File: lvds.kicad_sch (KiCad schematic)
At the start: 31 parts, among them J4 Conn_01x22_Female, J9 Conn_01x34_Female, U10 TPS61176RTER, U5 SN65DSI83TPAPRQ1

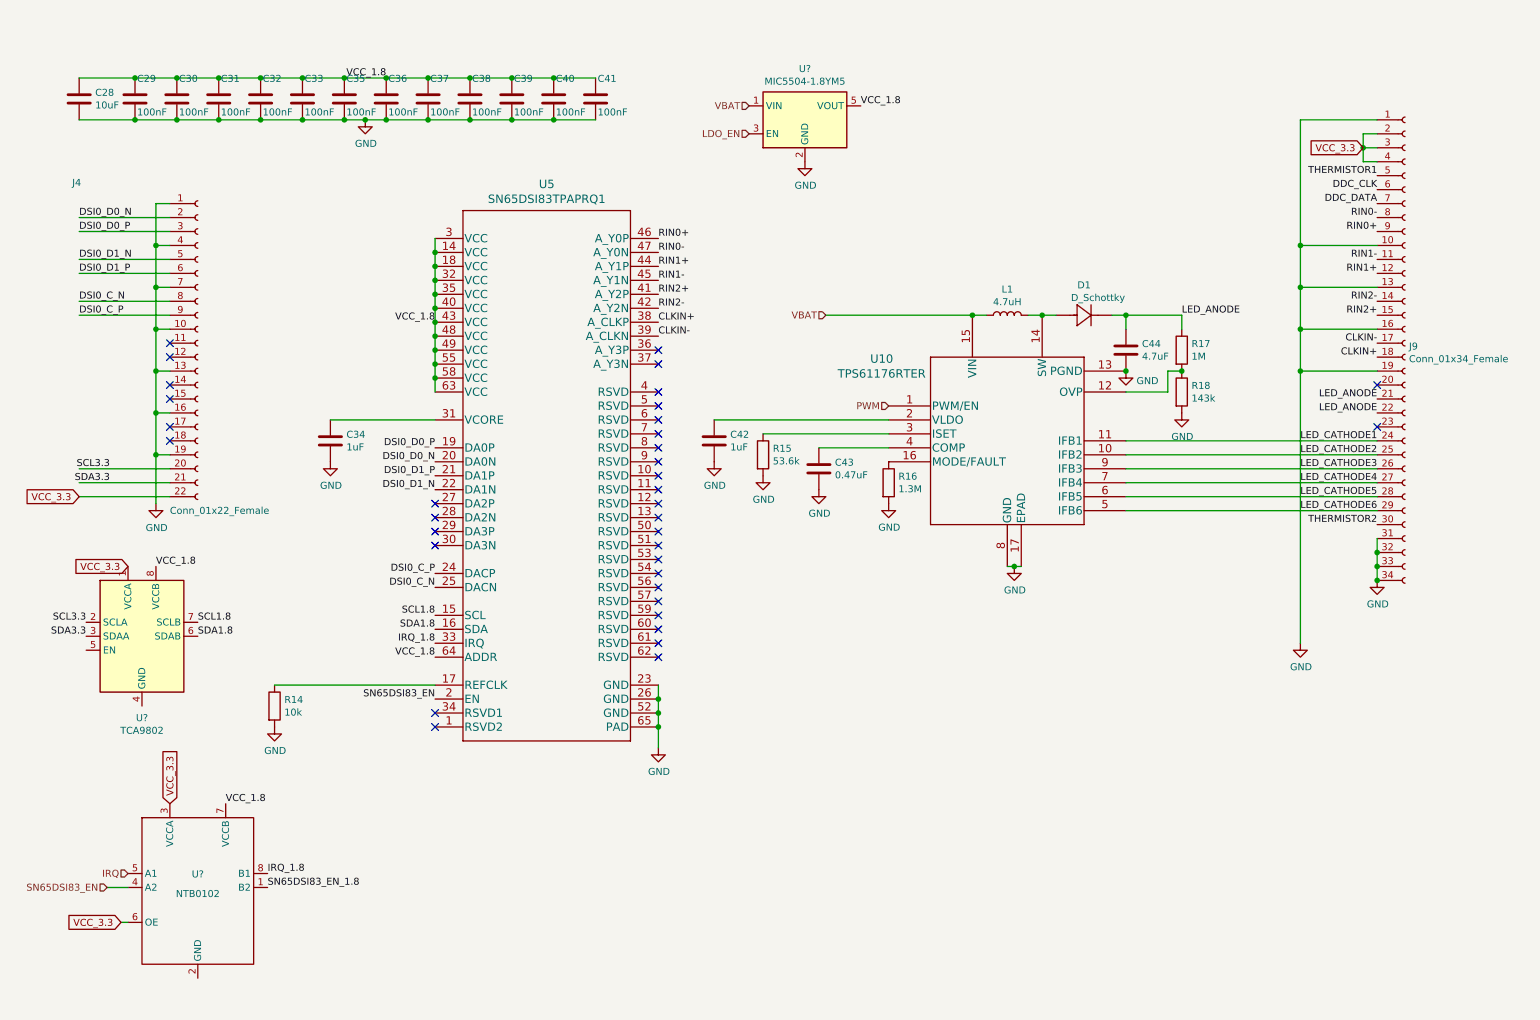
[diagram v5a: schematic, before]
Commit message: Import cm4_ipad_display_adapter.kicad_pcb into pipad.kicad_pcb, redraw LVDS diff pairs.
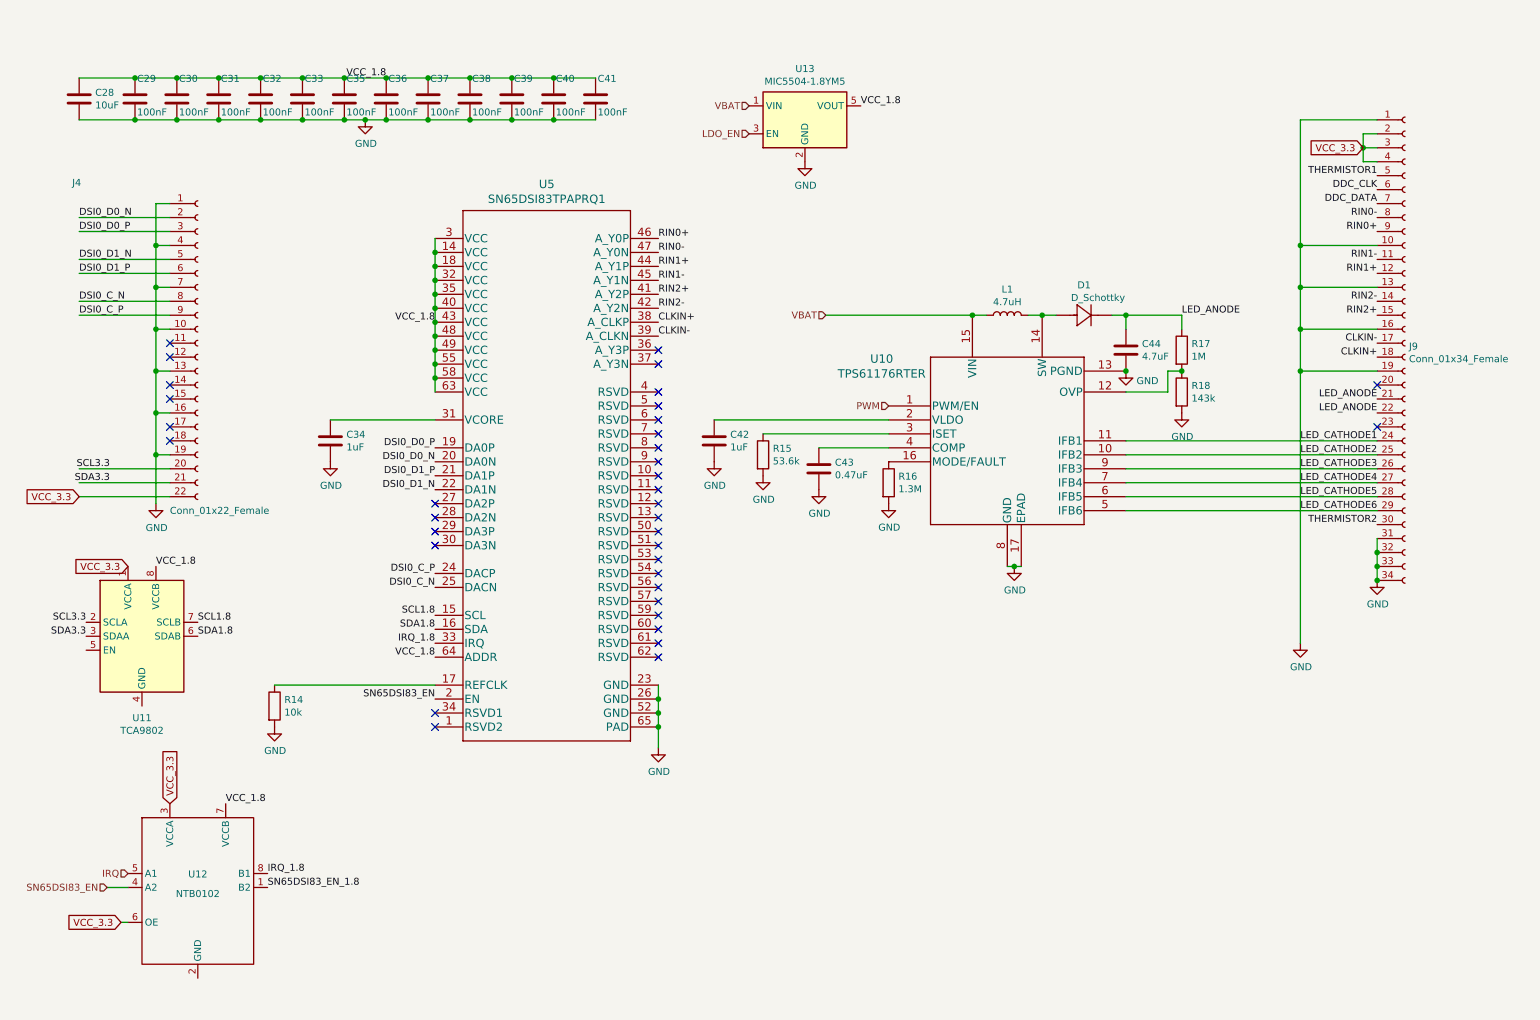
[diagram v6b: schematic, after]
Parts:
- U12: renamed from U?; footprint (none) -> Package_SO:TSSOP-8_3x3mm_P0.65mm
- gave numbers to parts that had none: 2
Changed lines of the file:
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@@
   (symbol (lib_id "power:GND") (at 157.48 36.83 0) (unit 1)
     (in_bom yes) (on_board yes)
-    (property "Reference" "#PWR?" (id 0) (at 157.48 43.18 0)
+    (property "Reference" "#PWR0121" (id 0) (at 157.48 43.18 0)
       (effects (font (size 1.27 1.27)) hide)
     )
@@
   (symbol (lib_id "Regulator_Linear:MIC5504-1.8YM5") (at 157.48 29.21 0) (unit 1)
     (in_bom yes) (on_board yes)
-    (property "Reference" "U?" (id 0) (at 157.48 19.9198 0))
+    (property "Reference" "U13" (id 0) (at 157.48 19.9198 0))
     (property "Value" "MIC5504-1.8YM5" (id 1) (at 157.48 22.2185 0))
     (property "Footprint" "Package_TO_SOT_SMD:SOT-23-5" (id 2) (at 157.48 39.37 0)
@@
   (symbol (lib_id "Interface:TCA9802") (at 36.83 123.19 0) (unit 1)
     (in_bom yes) (on_board yes) (fields_autoplaced)
-    (property "Reference" "U?" (id 0) (at 36.83 138.0554 0))
+    (property "Reference" "U11" (id 0) (at 36.83 138.0554 0))
     (property "Value" "TCA9802" (id 1) (at 36.83 140.3541 0))
     (property "Footprint" "Package_SO:VSSOP-8_3.0x3.0mm_P0.65mm" (id 2) (at 59.69 134.62 0)
@@
   (symbol (lib_id "NTB0102:NTB0102") (at 46.99 167.64 0) (unit 1)
     (in_bom yes) (on_board yes)
-    (property "Reference" "U?" (id 0) (at 46.99 166.4928 0))
+    (property "Reference" "U12" (id 0) (at 46.99 166.4928 0))
     (property "Value" "NTB0102" (id 1) (at 46.99 170.0615 0))
-    (property "Footprint" "" (id 2) (at 46.99 167.64 0)
-      (effects (font (size 1.27 1.27)) hide)
-    )
+    (property "Footprint" "Package_SO:TSSOP-8_3x3mm_P0.65mm" (id 2) (at 46.99 167.64 0)
+      (effects (font (size 1.27 1.27)) hide)
+    )

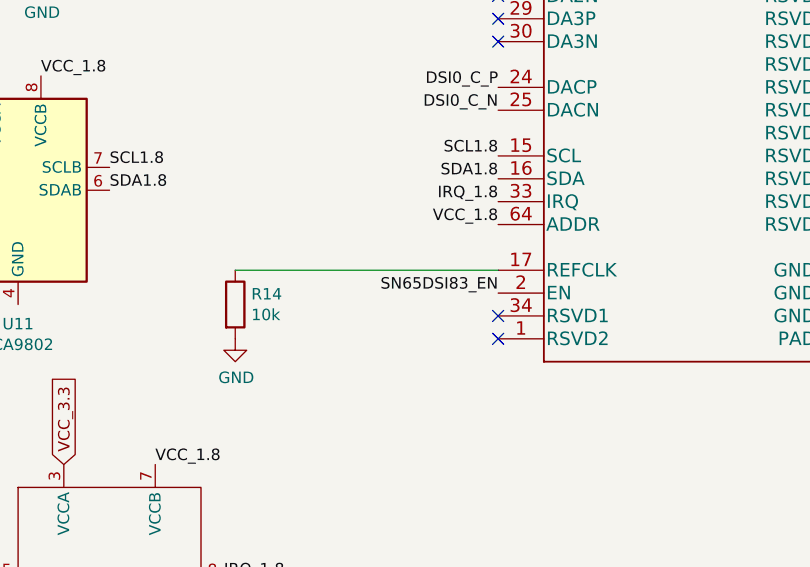
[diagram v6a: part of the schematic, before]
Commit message: Add dock connector, battery pads, and ambient light sensor/compass connector. Switch Pi GPIO header from from THT to SMT so it is easier to place/route. Route differential signals for LVDS converter.
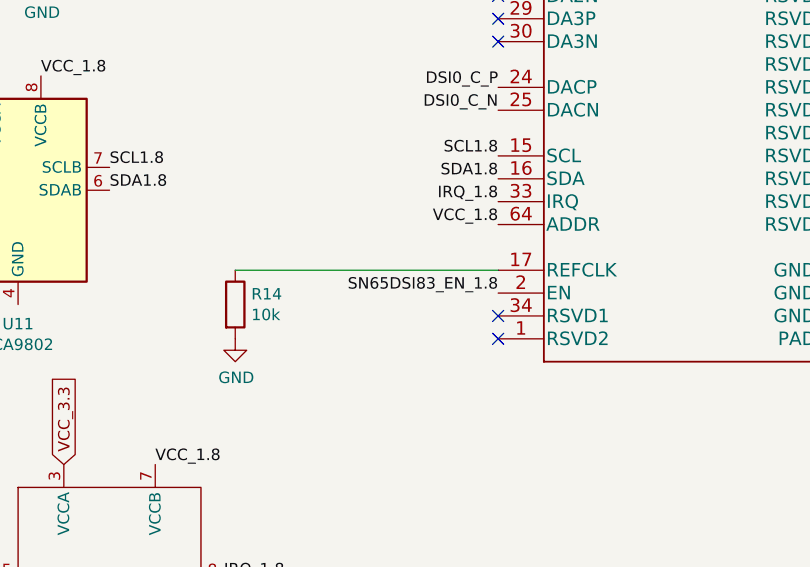
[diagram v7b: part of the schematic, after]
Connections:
- net SN65DSI83_EN: no longer U5.2 (EN)
- net SN65DSI83_EN_1.8: now also U5.2 (EN)
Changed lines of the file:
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@@
     (effects (font (size 1.27 1.27)) (justify right bottom))
   )
-  (label "SN65DSI83_EN" (at 90.17 134.62 180)
+  (label "SN65DSI83_EN_1.8" (at 90.17 134.62 180)
     (effects (font (size 1.27 1.27)) (justify right bottom))
   )

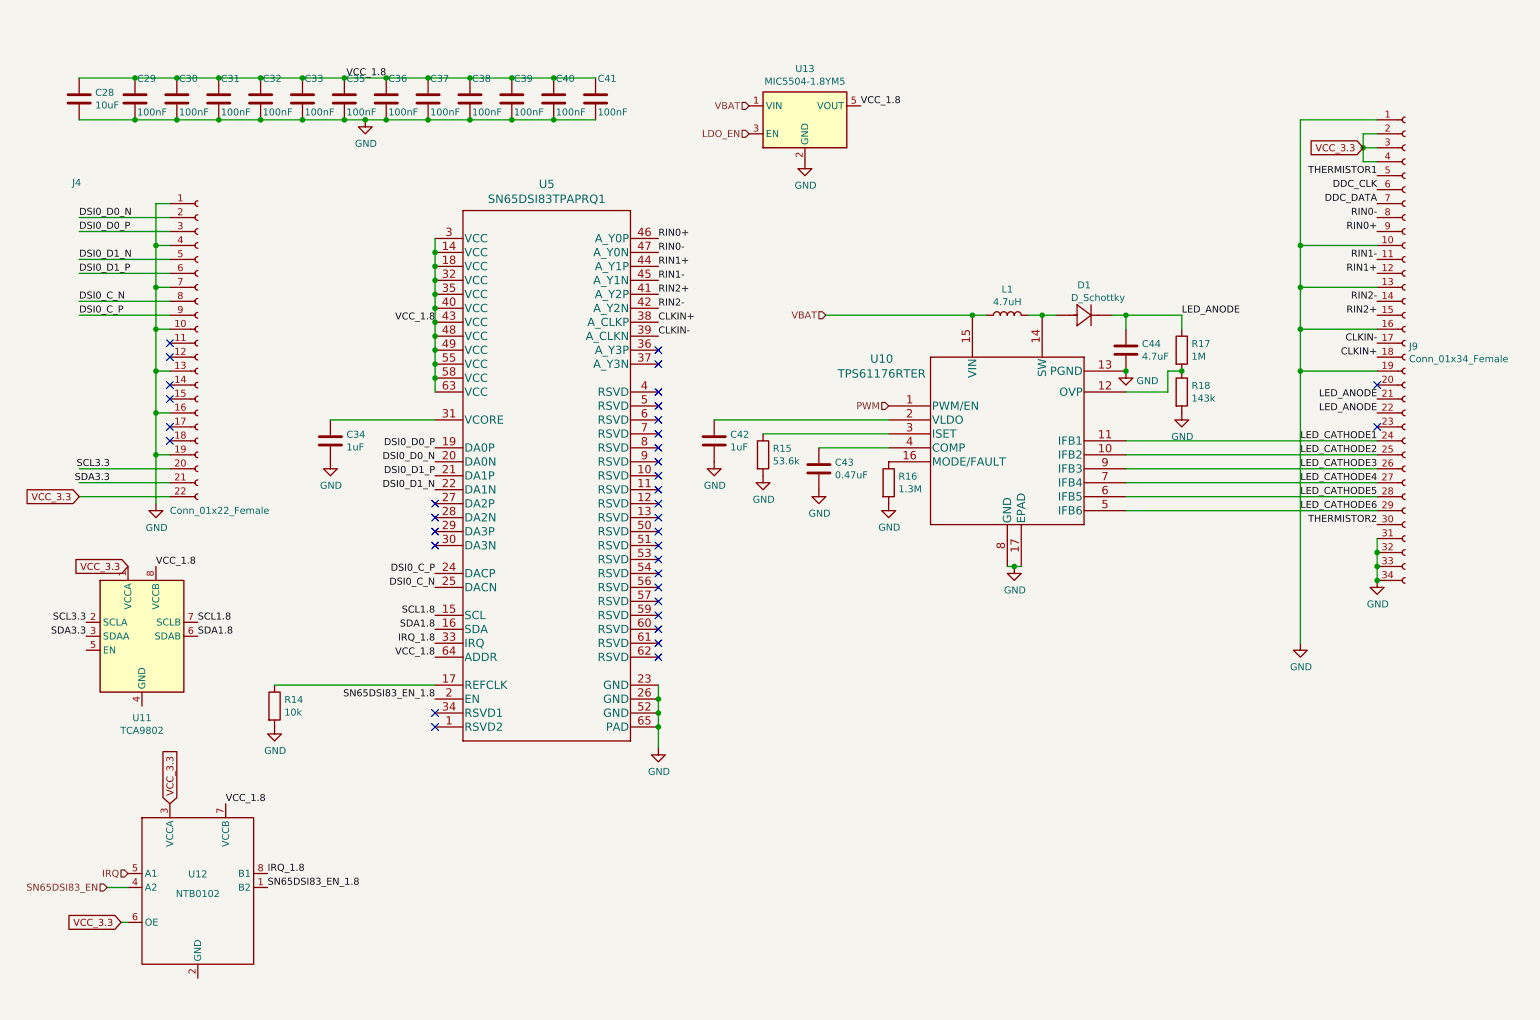
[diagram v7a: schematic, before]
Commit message: Change DSI connector to the 15-pin standard instead of 22-pin standard
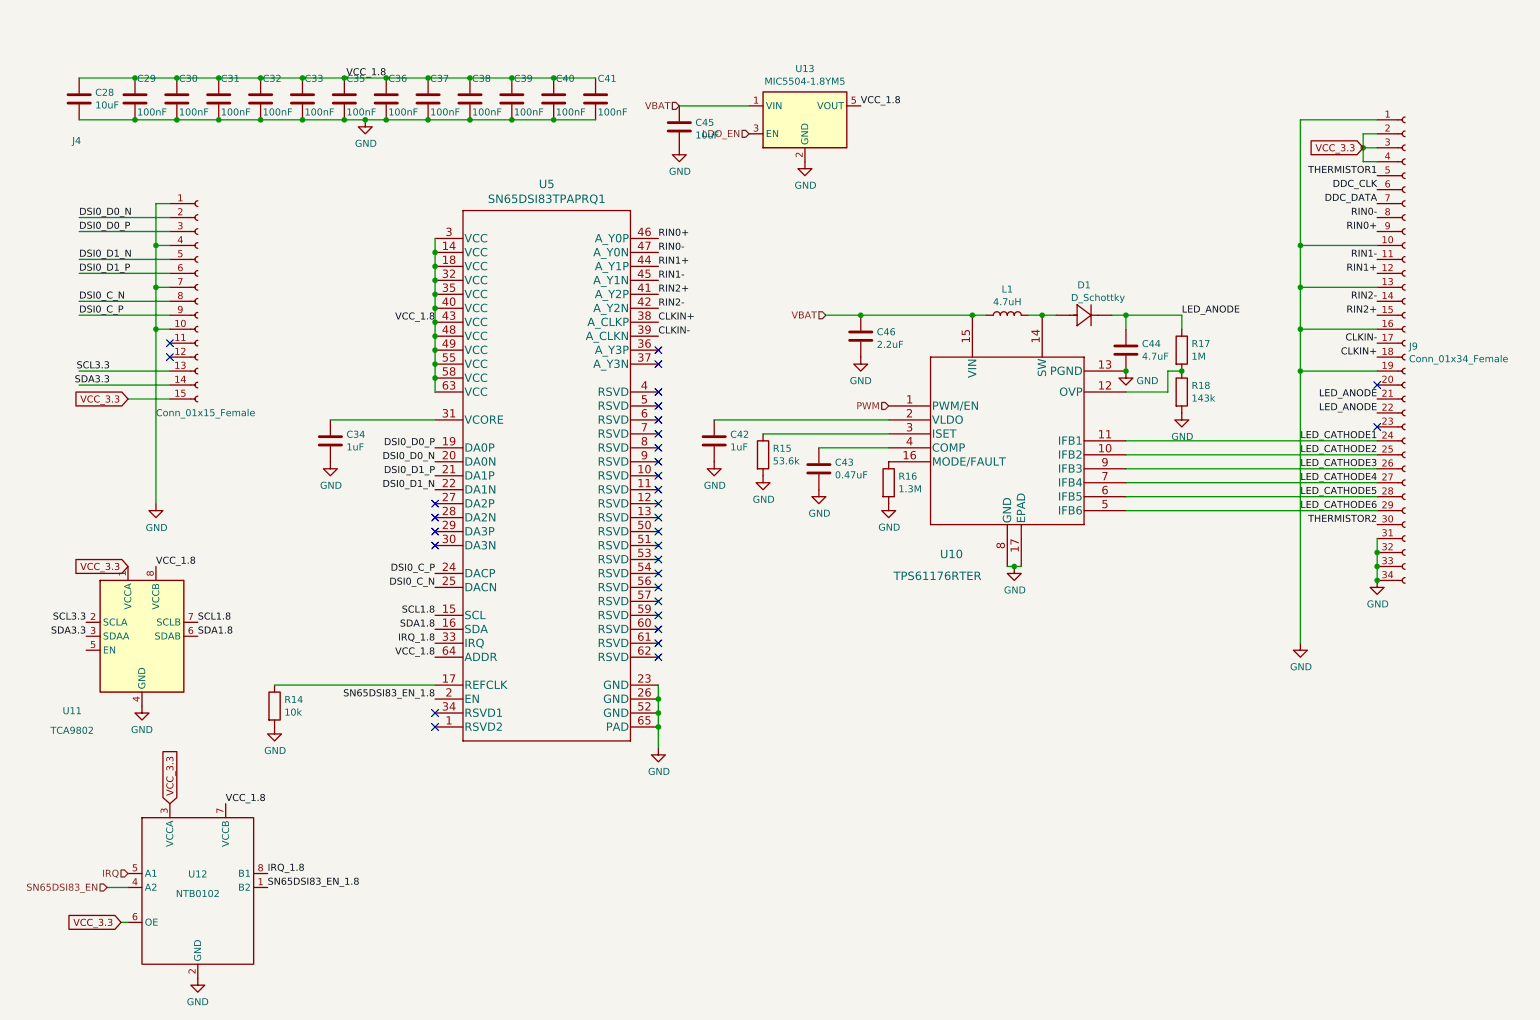
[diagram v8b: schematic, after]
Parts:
- added C45: 10uF, Capacitor_SMD:C_0402_1005Metric, symbol Device:C
- added C46: 2.2uF, Capacitor_SMD:C_0402_1005Metric, symbol Device:C
- C28, C29, C30, C31, C32, C33, C34, C35, C36, C37, C38, C39, C40, C41, C42, C43, C44: footprint Capacitor_SMD:C_0402_1005Metric_Pad0.74x0.62mm_HandSolder -> Capacitor_SMD:C_0402_1005Metric
- J4: value Conn_01x22_Female -> Conn_01x15_Female; footprint Connector_FFC-FPC:Hirose_FH12-22S-0.5SH_1x22-1MP_P0.50mm_Horizontal -> footprints:SFW15R-2STE1LF; symbol Connector:Conn_01x22_Female -> Connector:Conn_01x15_Female
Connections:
- net GND: now also U11.4 (GND), U12.2 (GND), C45.2, C46.2; no longer J4.13 (Pin_13), J4.16 (Pin_16), J4.19 (Pin_19)
- net SCL3.3: now also J4.13 (Pin_13); no longer J4.20 (Pin_20)
- net SDA3.3: now also J4.14 (Pin_14); no longer J4.21 (Pin_21)
- net VBAT: now also C45.1, C46.1
- net VCC_3.3: now also J4.15 (Pin_15); no longer J4.22 (Pin_22)
- no-connect marks 36 -> 32
